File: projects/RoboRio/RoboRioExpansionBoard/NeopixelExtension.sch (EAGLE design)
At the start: 6 parts

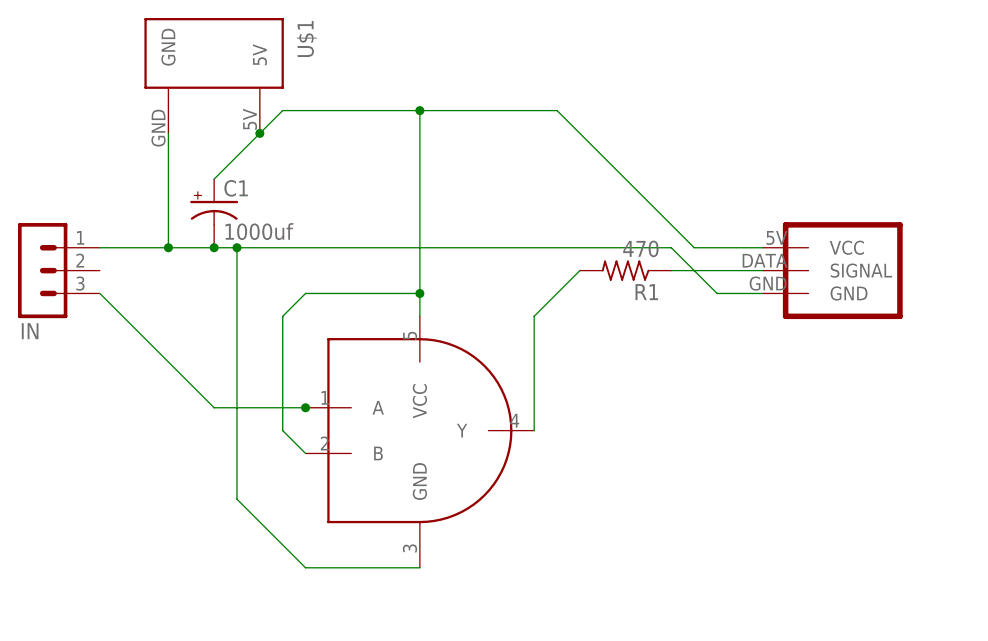
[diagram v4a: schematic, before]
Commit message: Updated neopixel board
still needs to have the planes come to .025 from the board edge
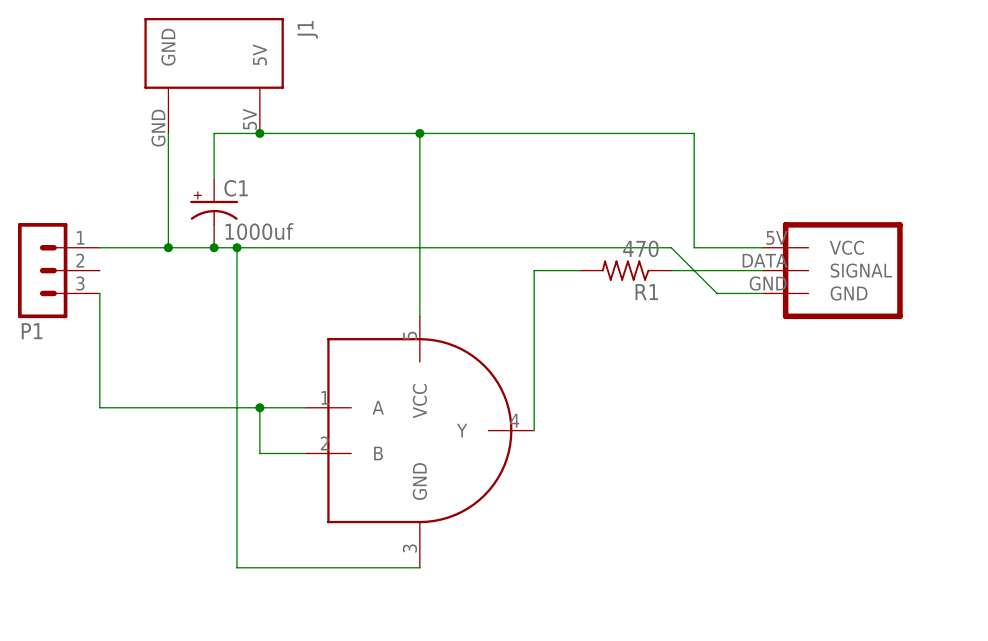
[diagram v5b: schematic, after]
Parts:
- R1: device resistor:R-US_0309/V -> resistor:R-US_R1206
- renumbered IN to P1, S1 to U1, U$1 to J1
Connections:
- removed net N$3: P1.3, U1.A
- new net N$2: P1.3, U1.A, U1.B
- net VCC: no longer U1.B

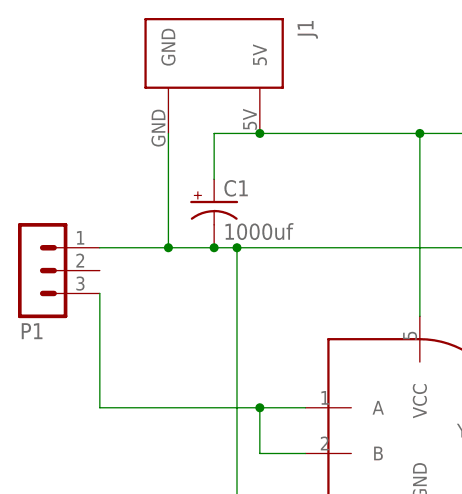
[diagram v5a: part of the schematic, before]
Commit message: Made sure Neopixel board could be fabricated
following a new DRU for midwestpcb
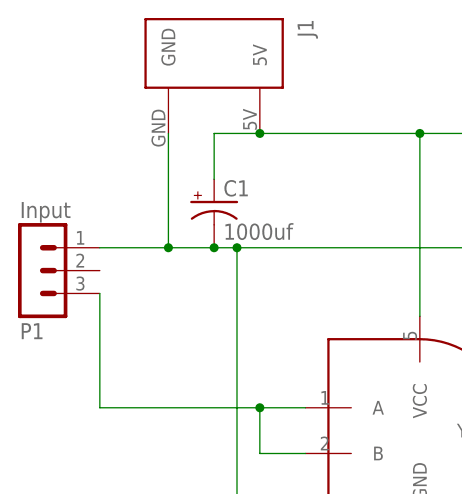
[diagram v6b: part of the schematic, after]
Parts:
- P1: value (none) -> Input
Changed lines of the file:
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@@
 <grid distance="0.1" unitdist="inch" unit="inch" style="lines" multiple="1" display="no" altdistance="0.01" altunitdist="inch" altunit="inch"/>
 <layers>
-<layer number="1" name="Top" color="4" fill="1" visible="yes" active="no"/>
-<layer number="16" name="Bottom" color="1" fill="1" visible="yes" active="no"/>
-<layer number="17" name="Pads" color="2" fill="1" visible="yes" active="no"/>
-<layer number="18" name="Vias" color="2" fill="1" visible="yes" active="no"/>
-<layer number="19" name="Unrouted" color="6" fill="1" visible="yes" active="no"/>
-<layer number="20" name="Dimension" color="15" fill="1" visible="yes" active="no"/>
-<layer number="21" name="tPlace" color="7" fill="1" visible="yes" active="no"/>
-<layer number="22" name="bPlace" color="7" fill="1" visible="yes" active="no"/>
-<layer number="23" name="tOrigins" color="15" fill="1" visible="yes" active="no"/>
-<layer number="24" name="bOrigins" color="15" fill="1" visible="yes" active="no"/>
-<layer number="25" name="tNames" color="7" fill="1" visible="yes" active="no"/>
-<layer number="26" name="bNames" color="7" fill="1" visible="yes" active="no"/>
-<layer number="27" name="tValues" color="7" fill="1" visible="yes" active="no"/>
-<layer number="28" name="bValues" color="7" fill="1" visible="yes" active="no"/>
+<layer number="1" name="Top" color="4" fill="1" visible="no" active="no"/>
+<layer number="16" name="Bottom" color="1" fill="1" visible="no" active="no"/>
+<layer number="17" name="Pads" color="2" fill="1" visible="no" active="no"/>
+<layer number="18" name="Vias" color="2" fill="1" visible="no" active="no"/>
+<layer number="19" name="Unrouted" color="6" fill="1" visible="no" active="no"/>
+<layer number="20" name="Dimension" color="15" fill="1" visible="no" active="no"/>
+<layer number="21" name="tPlace" color="7" fill="1" visible="no" active="no"/>
+<layer number="22" name="bPlace" color="7" fill="1" visible="no" active="no"/>
+<layer number="23" name="tOrigins" color="15" fill="1" visible="no" active="no"/>
+<layer number="24" name="bOrigins" color="15" fill="1" visible="no" active="no"/>
+<layer number="25" name="tNames" color="7" fill="1" visible="no" active="no"/>
+<layer number="26" name="bNames" color="7" fill="1" visible="no" active="no"/>
+<layer number="27" name="tValues" color="7" fill="1" visible="no" active="no"/>
+<layer number="28" name="bValues" color="7" fill="1" visible="no" active="no"/>
 <layer number="29" name="tStop" color="7" fill="3" visible="no" active="no"/>
 <layer number="30" name="bStop" color="7" fill="6" visible="no" active="no"/>
@@
 <layer number="35" name="tGlue" color="7" fill="4" visible="no" active="no"/>
 <layer number="36" name="bGlue" color="7" fill="5" visible="no" active="no"/>
-<layer number="37" name="tTest" color="7" fill="1" visible="yes" active="no"/>
-<layer number="38" name="bTest" color="7" fill="1" visible="yes" active="no"/>
+<layer number="37" name="tTest" color="7" fill="1" visible="no" active="no"/>
+<layer number="38" name="bTest" color="7" fill="1" visible="no" active="no"/>
 <layer number="39" name="tKeepout" color="4" fill="11" visible="no" active="no"/>
 <layer number="40" name="bKeepout" color="1" fill="11" visible="no" active="no"/>
@@
 <layer number="44" name="Drills" color="7" fill="1" visible="no" active="no"/>
 <layer number="45" name="Holes" color="7" fill="1" visible="no" active="no"/>
-<layer number="46" name="Milling" color="3" fill="1" visible="yes" active="no"/>
-<layer number="47" name="Measures" color="7" fill="1" visible="yes" active="no"/>
-<layer number="48" name="Document" color="7" fill="1" visible="yes" active="no"/>
-<layer number="49" name="Reference" color="7" fill="1" visible="yes" active="no"/>
-<layer number="50" name="dxf" color="7" fill="1" visible="yes" active="no"/>
-<layer number="51" name="tDocu" color="7" fill="1" visible="yes" active="no"/>
-<layer number="52" name="bDocu" color="7" fill="1" visible="yes" active="no"/>
-<layer number="53" name="tGND_GNDA" color="7" fill="9" visible="yes" active="no"/>
-<layer number="54" name="bGND_GNDA" color="1" fill="9" visible="yes" active="no"/>
-<layer number="56" name="wert" color="7" fill="1" visible="yes" active="no"/>
-<layer number="57" name="tCAD" color="7" fill="1" visible="yes" active="no"/>
+<layer number="46" name="Milling" color="3" fill="1" visible="no" active="no"/>
+<layer number="47" name="Measures" color="7" fill="1" visible="no" active="no"/>
+<layer number="48" name="Document" color="7" fill="1" visible="no" active="no"/>
+<layer number="49" name="Reference" color="7" fill="1" visible="no" active="no"/>
+<layer number="50" name="dxf" color="7" fill="1" visible="no" active="no"/>
+<layer number="51" name="tDocu" color="7" fill="1" visible="no" active="no"/>
+<layer number="52" name="bDocu" color="7" fill="1" visible="no" active="no"/>
+<layer number="53" name="tGND_GNDA" color="7" fill="9" visible="no" active="no"/>
+<layer number="54" name="bGND_GNDA" color="1" fill="9" visible="no" active="no"/>
+<layer number="56" name="wert" color="7" fill="1" visible="no" active="no"/>
+<layer number="57" name="tCAD" color="7" fill="1" visible="no" active="no"/>
 <layer number="90" name="Modules" color="5" fill="1" visible="yes" active="yes"/>
 <layer number="91" name="Nets" color="2" fill="1" visible="yes" active="yes"/>
@@
 <parts>
 <part name="R1" library="resistor" deviceset="R-US_" device="R1206" value="470"/>
-<part name="P1" library="con-lstb-modified" deviceset="MA03-1" device=""/>
+<part name="P1" library="con-lstb-modified" deviceset="MA03-1" device="" value="Input"/>
 <part name="C1" library="adafruit" deviceset="CPOL-US" device="E5-10.5" value="1000uf"/>
 <part name="J1" library="Molex-39543-0002" deviceset="POWER" device=""/>
